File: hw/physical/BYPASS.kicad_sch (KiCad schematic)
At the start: 13 parts

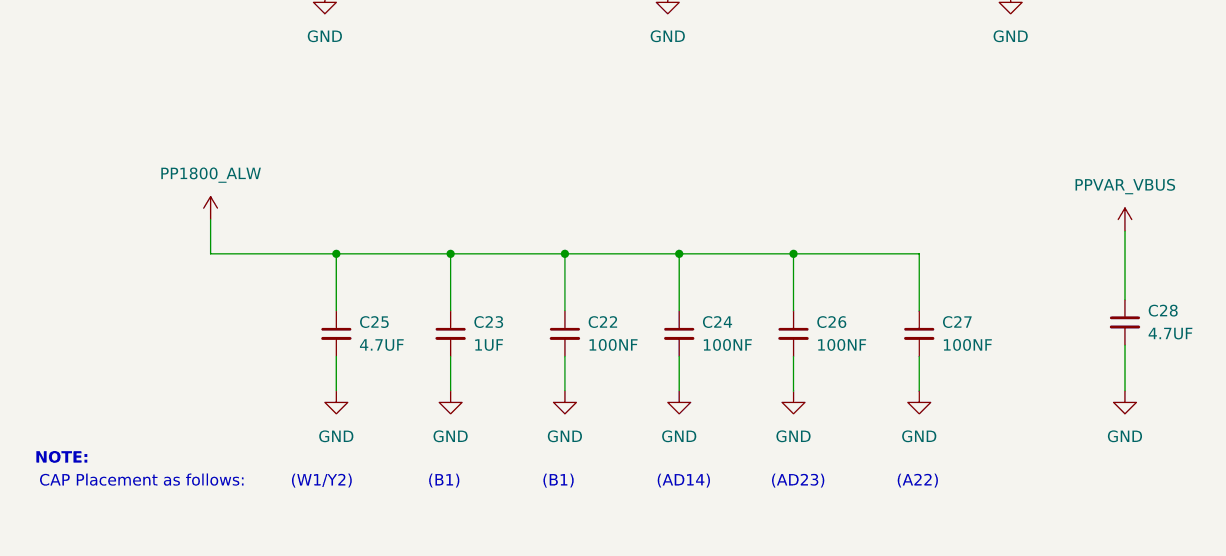
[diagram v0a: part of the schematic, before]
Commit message: Adding nRF54L10 schematic library component. Redrew MCU page with nRF54L10 and rearranged or changed net labels and global labels.
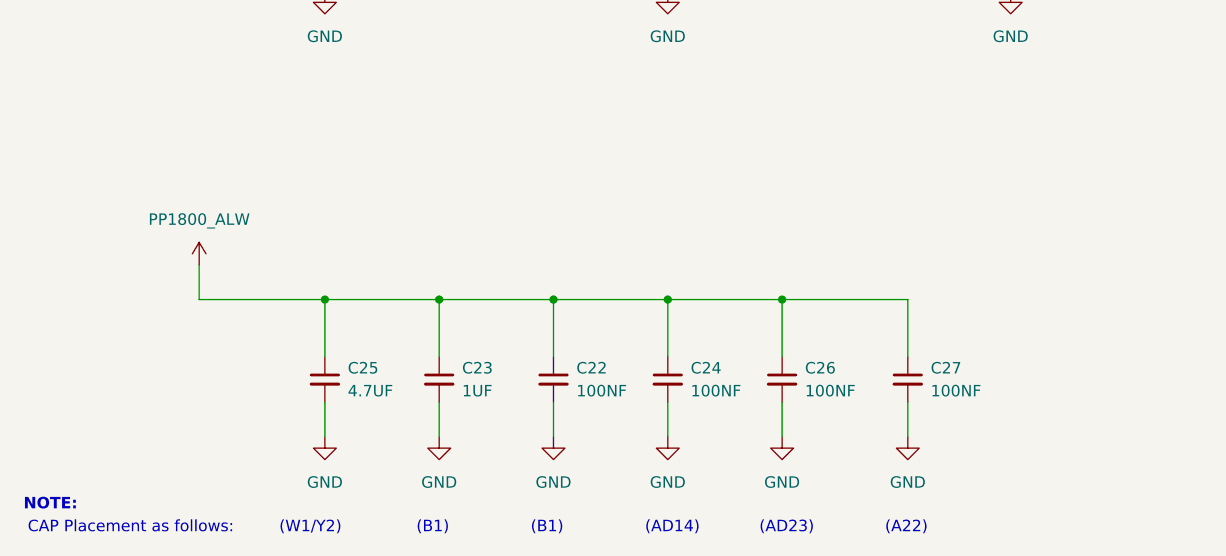
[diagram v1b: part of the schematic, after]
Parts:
- removed C28: 4.7UF, symbol Device:C_Small
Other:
- moved on the sheet: C22, C23, C24, C25, C26, C27

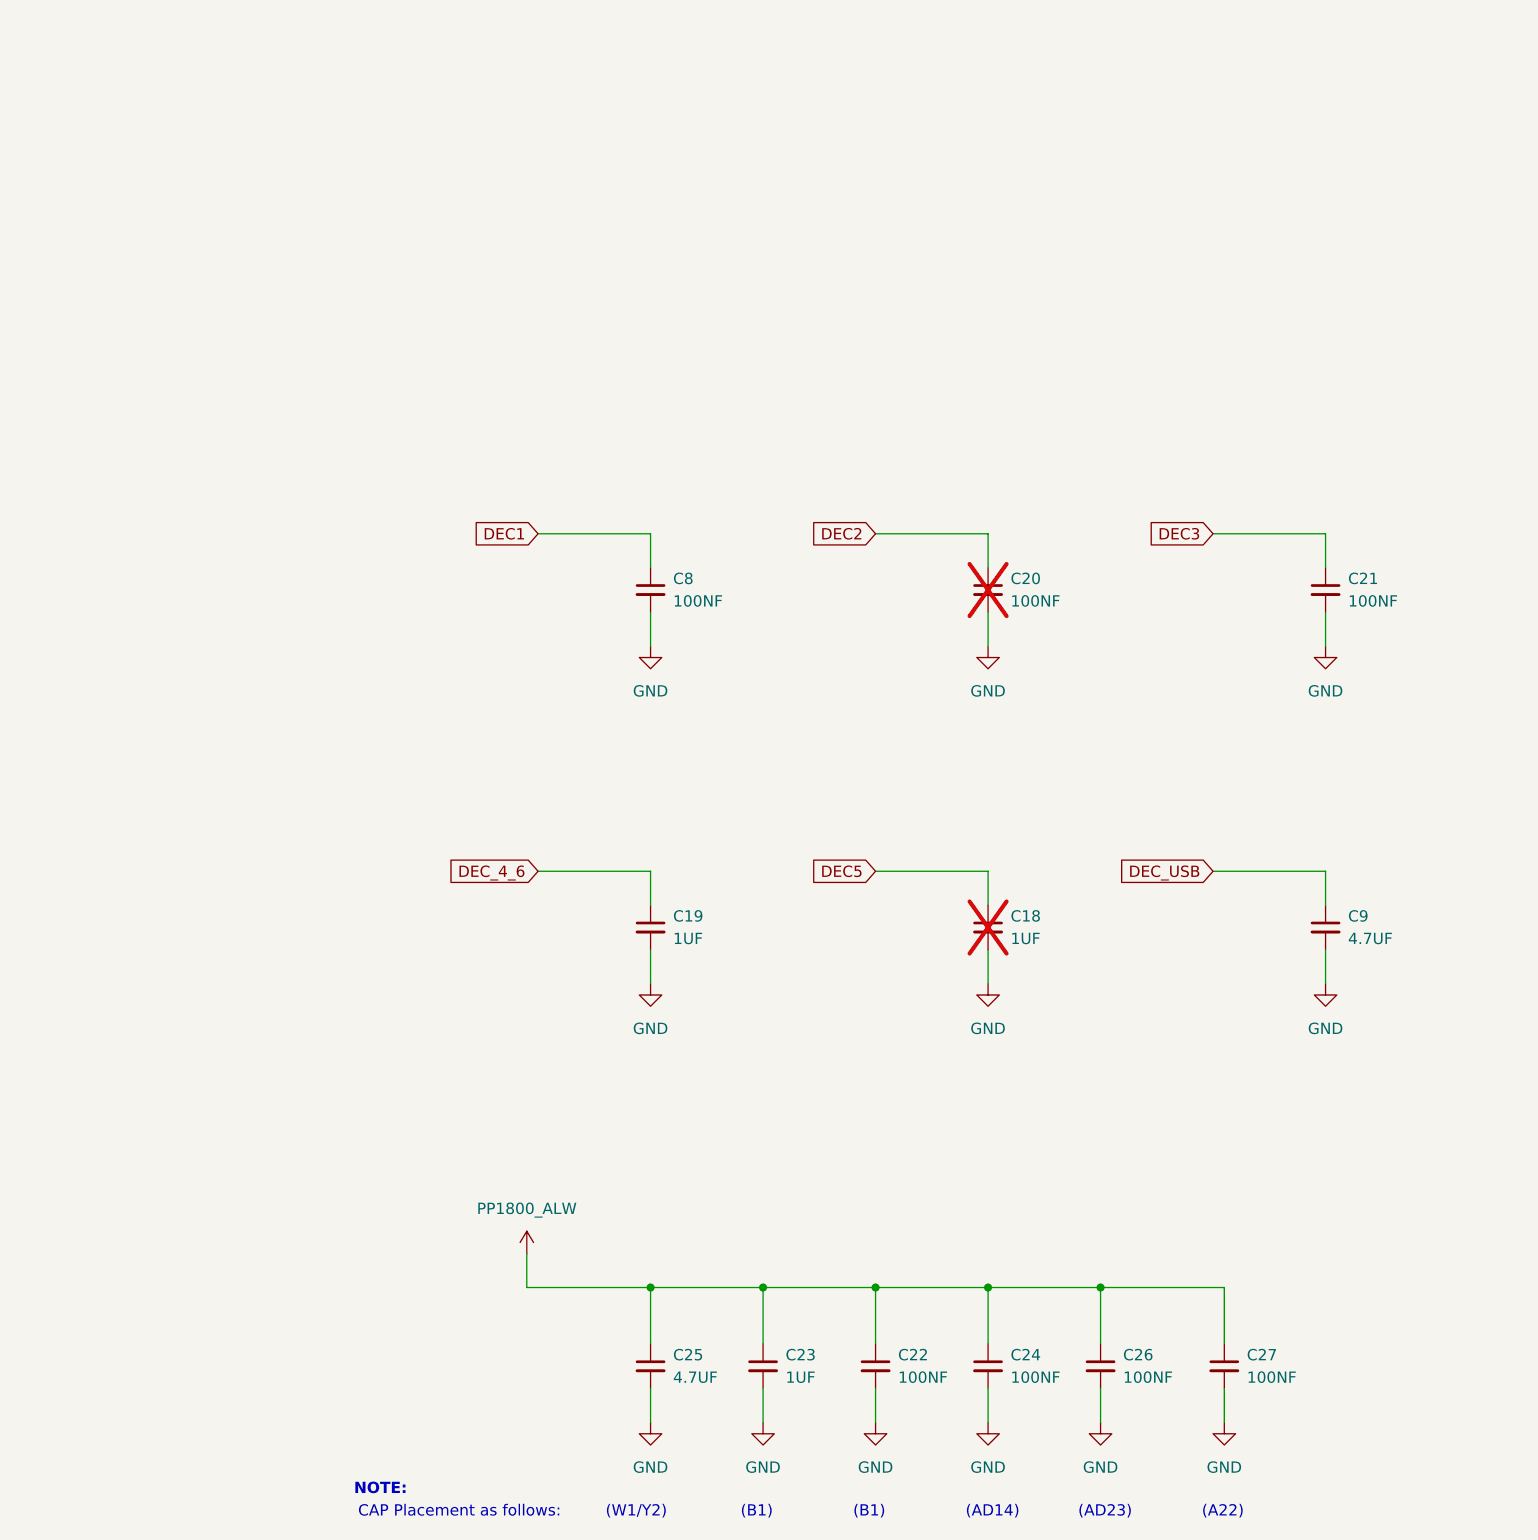
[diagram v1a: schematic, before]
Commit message: Various Schematic Modifications and Additions. * Removed Bypass page and moved bypass caps to MCU page. * Moved MCU VSS_PA pin to logical location as per Nordic guidelines. * Added Display Circuit, level shifters, charge pump, connector, etc. * Added 3.3V display VREG with Enable GPIO. * Added BLE RF components as per Nordic guidelines. * Added DCC circuit as per Nordic guidelines. * Rearranged GPIO's and interfaces. * Fixed various schematic errors.
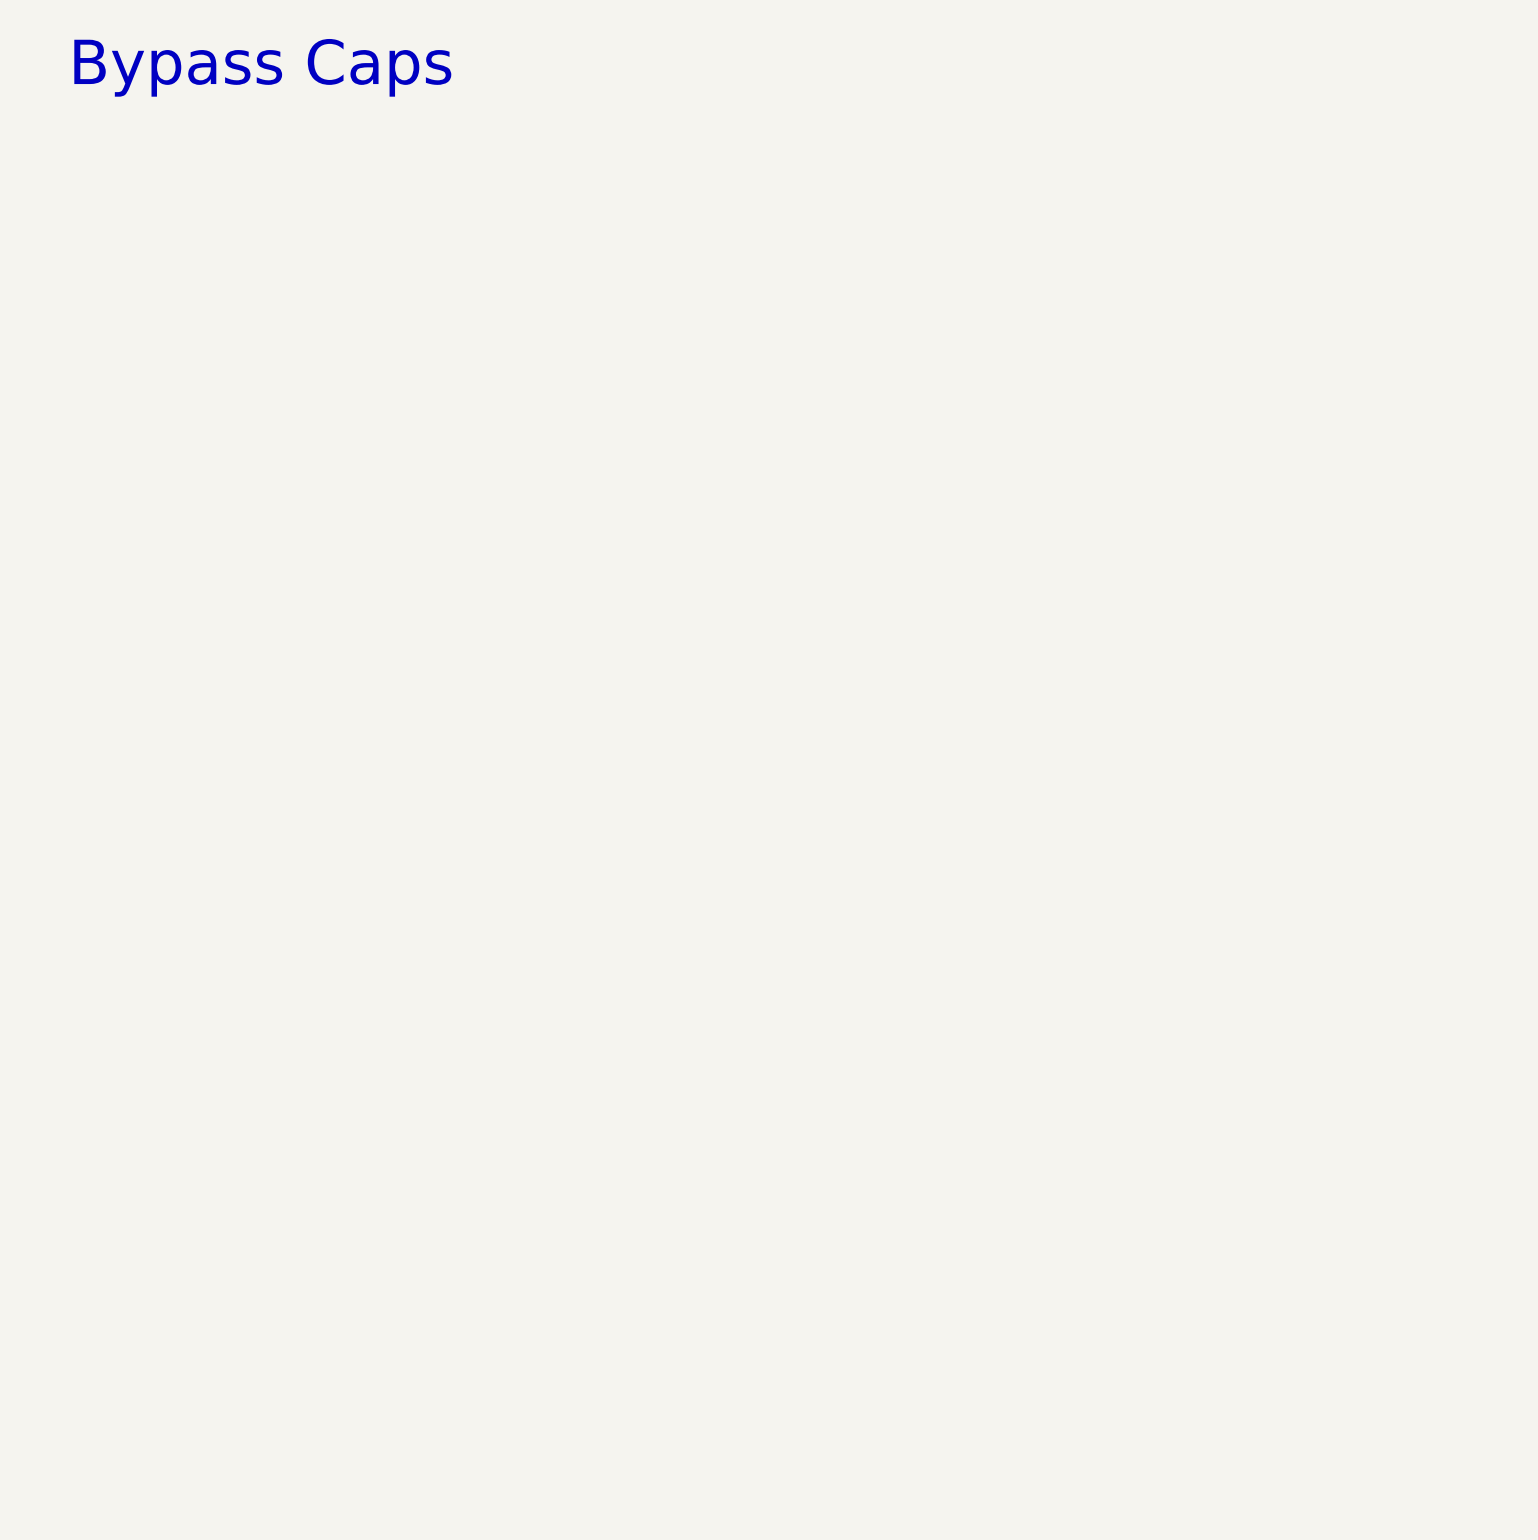
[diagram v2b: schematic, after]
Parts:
- removed C18, C19, C23: 1UF, symbol Device:C_Small
- removed C20, C21, C22, C24, C26, C27, C8: 100NF, symbol Device:C_Small
- removed C25, C9: 4.7UF, symbol Device:C_Small
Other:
- note added: "Bypass Caps"
- note removed: "(A22)"
- note removed: "(AD14)"
- note removed: "(AD23)"
- note removed: "(B1)"
- note removed: "(W1/Y2)"
- note removed: "CAP Placement as follows:"
- note removed: "NOTE:"
